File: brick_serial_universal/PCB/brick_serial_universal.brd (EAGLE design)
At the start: 25.4 x 33 mm, 12 parts

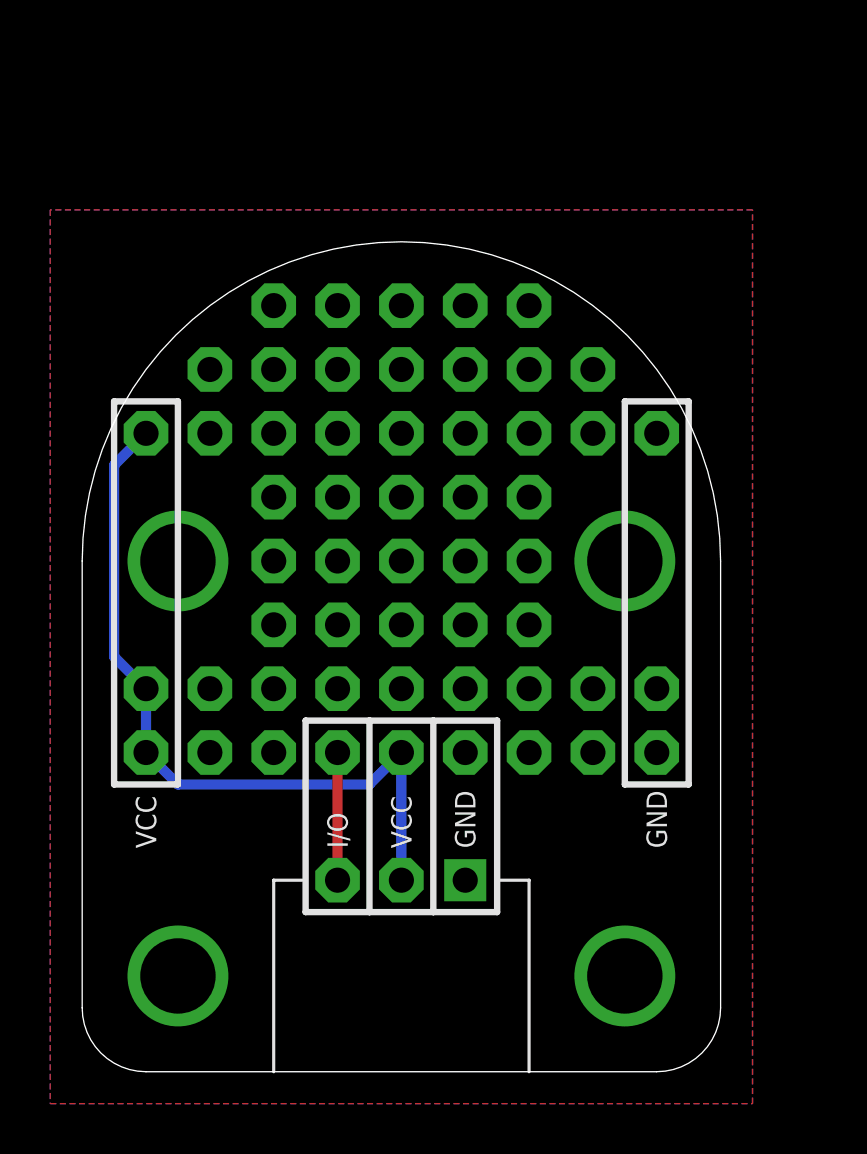
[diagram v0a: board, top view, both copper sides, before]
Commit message: add brick_universal
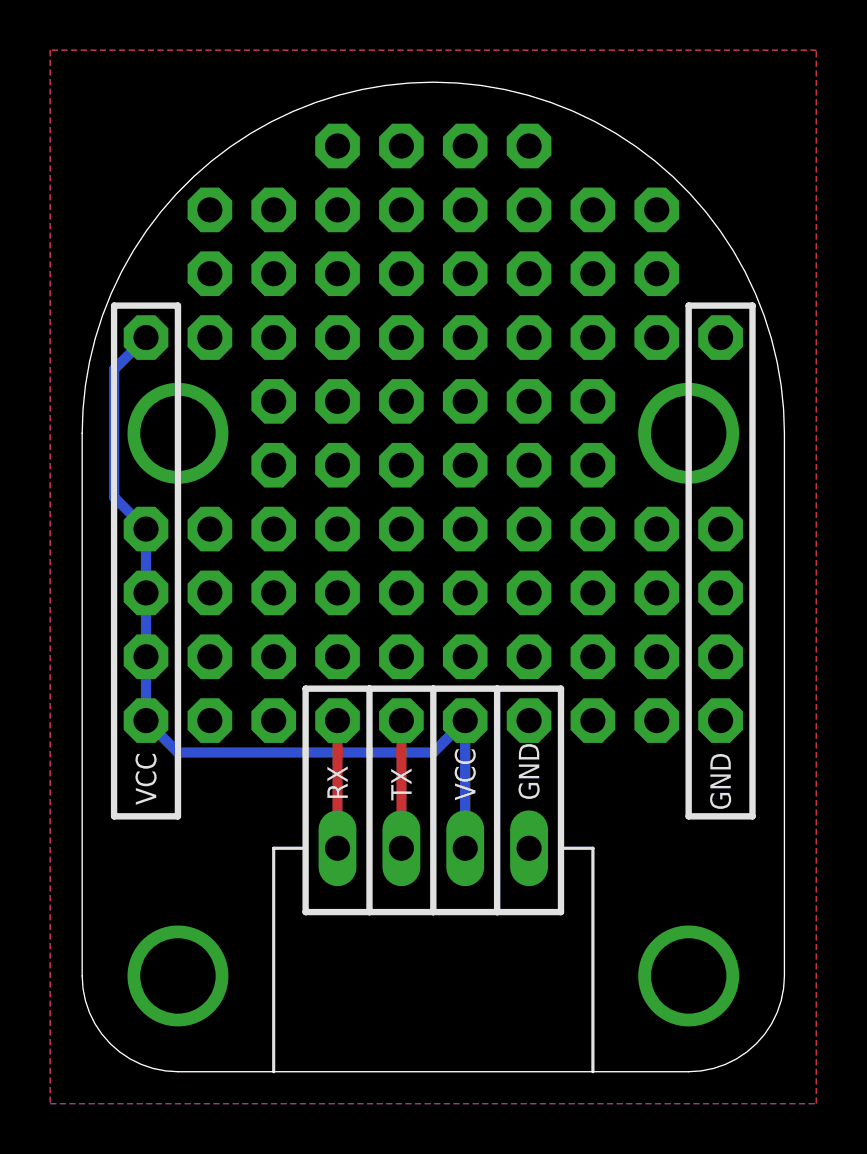
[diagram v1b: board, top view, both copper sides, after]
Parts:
- removed U$1: (no value), FaBo-etc:LOGO_OSHW_S_BOTTOM
- added J11, J12, J13, J14, J15: (no value), FaBo-etc:PIN_1X1_NONAME
- added U$2: (no value), FaBo-etc:LOGO_OSHW_S_BOTTOM
- J1: device FaBo-Template:FABO_BRICK_3PIN_UNIVERSAL -> FaBo-Template:FABO_BRICK_SERIAL_UNIVERSAL
- moved J9 24.7 mm to (2.54, 29.2)
- moved J8 22.2 mm to (2.54, 21.6)
- moved J7 14.2 mm to (2.54, 19.1)
- moved J4 12.8 mm to (15.2, 14.0)
- moved J6 8.89 mm to (2.54, 16.5)
- moved J10 4.58 mm to (25.4, 29.2)
- moved J1 2.84 mm to (14.0, 19.1)
- moved J2 1.27 mm to (10.2, 14.0)
- moved J3 1.27 mm to (12.7, 14.0)
- moved U$3 1.27 mm to (14.0, 2.54)
- moved J5 1.27 mm to (2.54, 14.0)
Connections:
- removed net IO: J1.IN/OUT, J2.1
- new net RX: J1.RX, J2.1
- new net TX: J1.TX, J3.1
- net GND: now also J11.1, J12.1, J13.1, J14.1, J15.1; no longer J7.1, J8.1, J9.1
- net VCC: now also J7.1, J8.1, J9.1; no longer J3.1
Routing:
- net VCC: track 30.0 -> 35.1 mm
- net TX: track 0.00 -> 5.08 mm
- net RX: track 0.00 -> 5.08 mm
- net IO: track 5.08 -> 0.00 mm
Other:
- board size 25.4 x 33 mm -> 27.9 x 39.4 mm
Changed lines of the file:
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@@
 <board>
 <plain>
+<text x="13.97" y="1.27" size="1.016" layer="22" font="vector" ratio="12" rot="MR0" align="bottom-center">MADE IN JAPAN</text>
+<text x="2.54" y="12.7" size="0.8128" layer="21" font="vector" ratio="12" rot="R270" align="center-left">VCC</text>
+<text x="25.4" y="12.7" size="0.8128" layer="21" font="vector" ratio="12" rot="R270" align="center-left">GND</text>
+<wire x1="8.89" y1="6.35" x2="8.89" y2="15.24" width="0.254" layer="21"/>
+<wire x1="8.89" y1="15.24" x2="11.43" y2="15.24" width="0.254" layer="21"/>
+<wire x1="11.43" y1="15.24" x2="13.97" y2="15.24" width="0.254" layer="21"/>
+<wire x1="13.97" y1="15.24" x2="16.51" y2="15.24" width="0.254" layer="21"/>
+<wire x1="16.51" y1="15.24" x2="19.05" y2="15.24" width="0.254" layer="21"/>
+<wire x1="19.05" y1="15.24" x2="19.05" y2="6.35" width="0.254" layer="21"/>
+<wire x1="19.05" y1="6.35" x2="16.51" y2="6.35" width="0.254" layer="21"/>
 <wire x1="16.51" y1="6.35" x2="13.97" y2="6.35" width="0.254" layer="21"/>
 <wire x1="13.97" y1="6.35" x2="11.43" y2="6.35" width="0.254" layer="21"/>
 <wire x1="11.43" y1="6.35" x2="8.89" y2="6.35" width="0.254" layer="21"/>
-<wire x1="8.89" y1="6.35" x2="8.89" y2="13.97" width="0.254" layer="21"/>
-<wire x1="8.89" y1="13.97" x2="11.43" y2="13.97" width="0.254" layer="21"/>
-<wire x1="11.43" y1="13.97" x2="13.97" y2="13.97" width="0.254" layer="21"/>
-<wire x1="13.97" y1="13.97" x2="16.51" y2="13.97" width="0.254" layer="21"/>
-<wire x1="16.51" y1="13.97" x2="16.51" y2="6.35" width="0.254" layer="21"/>
-<wire x1="13.97" y1="13.97" x2="13.97" y2="6.35" width="0.254" layer="21"/>
-<wire x1="11.43" y1="13.97" x2="11.43" y2="6.35" width="0.254" layer="21"/>
-<wire x1="3.81" y1="26.67" x2="3.81" y2="11.43" width="0.254" layer="21"/>
-<wire x1="3.81" y1="11.43" x2="1.27" y2="11.43" width="0.254" layer="21"/>
-<wire x1="1.27" y1="11.43" x2="1.27" y2="26.67" width="0.254" layer="21"/>
-<wire x1="1.27" y1="26.67" x2="3.81" y2="26.67" width="0.254" layer="21"/>
-<wire x1="21.59" y1="26.67" x2="24.13" y2="26.67" width="0.254" layer="21"/>
-<wire x1="24.13" y1="26.67" x2="24.13" y2="11.43" width="0.254" layer="21"/>
-<wire x1="24.13" y1="11.43" x2="21.59" y2="11.43" width="0.254" layer="21"/>
-<wire x1="21.59" y1="11.43" x2="21.59" y2="26.67" width="0.254" layer="21"/>
-<text x="22.86" y="8.89" size="0.8128" layer="21" font="vector" ratio="12" rot="R90" align="center-left">GND</text>
-<text x="2.54" y="8.89" size="0.8128" layer="21" font="vector" ratio="12" rot="R90" align="center-left">VCC</text>
-<text x="12.7" y="1.27" size="1.016" layer="22" font="vector" ratio="12" rot="MR0" align="bottom-center">MADE IN JAPAN</text>
+<wire x1="11.43" y1="15.24" x2="11.43" y2="6.35" width="0.254" layer="21"/>
+<wire x1="13.97" y1="15.24" x2="13.97" y2="6.35" width="0.254" layer="21"/>
+<wire x1="16.51" y1="15.24" x2="16.51" y2="6.35" width="0.254" layer="21"/>
+<wire x1="24.13" y1="30.48" x2="26.67" y2="30.48" width="0.254" layer="21"/>
+<wire x1="26.67" y1="30.48" x2="26.67" y2="10.16" width="0.254" layer="21"/>
+<wire x1="26.67" y1="10.16" x2="24.13" y2="10.16" width="0.254" layer="21"/>
+<wire x1="24.13" y1="10.16" x2="24.13" y2="30.48" width="0.254" layer="21"/>
+<wire x1="1.27" y1="30.48" x2="3.81" y2="30.48" width="0.254" layer="21"/>
+<wire x1="3.81" y1="30.48" x2="3.81" y2="10.16" width="0.254" layer="21"/>
+<wire x1="3.81" y1="10.16" x2="1.27" y2="10.16" width="0.254" layer="21"/>
+<wire x1="1.27" y1="10.16" x2="1.27" y2="30.48" width="0.254" layer="21"/>
 </plain>
 <attributes>
@@
 </autorouter>
 <elements>
-<element name="J1" library="FaBo-Template" package="FABO_BRICK_3PIN_UNIVERSAL" value="" x="12.7" y="16.51"/>
-<element name="J2" library="FaBo-etc" package="PIN_1X1_NONAME" value="" x="10.16" y="12.7"/>
-<element name="J3" library="FaBo-etc" package="PIN_1X1_NONAME" value="" x="12.7" y="12.7"/>
-<element name="J4" library="FaBo-etc" package="PIN_1X1_NONAME" value="" x="2.54" y="12.7"/>
-<element name="J5" library="FaBo-etc" package="PIN_1X1_NONAME" value="" x="2.54" y="15.24"/>
-<element name="J6" library="FaBo-etc" package="PIN_1X1_NONAME" value="" x="2.54" y="25.4"/>
-<element name="J7" library="FaBo-etc" package="PIN_1X1_NONAME" value="" x="15.24" y="12.7"/>
-<element name="J8" library="FaBo-etc" package="PIN_1X1_NONAME" value="" x="22.86" y="12.7"/>
-<element name="J9" library="FaBo-etc" package="PIN_1X1_NONAME" value="" x="22.86" y="15.24"/>
-<element name="J10" library="FaBo-etc" package="PIN_1X1_NONAME" value="" x="22.86" y="25.4"/>
-<element name="U$1" library="FaBo-etc" package="LOGO_OSHW_S_BOTTOM" value="" x="21.59" y="8.89"/>
-<element name="U$3" library="FaBo-etc" package="LOGO_FABO_M_BOTTOM" value="" x="12.7" y="2.54"/>
+<element name="J1" library="FaBo-Template" package="FABO_BRICK_SERIAL_UNIVERSAL" value="" x="13.97" y="19.05"/>
+<element name="J10" library="FaBo-etc" package="PIN_1X1_NONAME" value="" x="25.4" y="29.21"/>
+<element name="J11" library="FaBo-etc" package="PIN_1X1_NONAME" value="" x="25.4" y="21.59"/>
+<element name="J12" library="FaBo-etc" package="PIN_1X1_NONAME" value="" x="25.4" y="19.05"/>
+<element name="J13" library="FaBo-etc" package="PIN_1X1_NONAME" value="" x="17.78" y="13.97"/>
+<element name="J14" library="FaBo-etc" package="PIN_1X1_NONAME" value="" x="25.4" y="13.97"/>
+<element name="J15" library="FaBo-etc" package="PIN_1X1_NONAME" value="" x="25.4" y="16.51"/>
+<element name="J2" library="FaBo-etc" package="PIN_1X1_NONAME" value="" x="10.16" y="13.97"/>
+<element name="J3" library="FaBo-etc" package="PIN_1X1_NONAME" value="" x="12.7" y="13.97"/>
+<element name="J4" library="FaBo-etc" package="PIN_1X1_NONAME" value="" x="15.24" y="13.97"/>
+<element name="J5" library="FaBo-etc" package="PIN_1X1_NONAME" value="" x="2.54" y="13.97"/>
+<element name="J6" library="FaBo-etc" package="PIN_1X1_NONAME" value="" x="2.54" y="16.51"/>
+<element name="J7" library="FaBo-etc" package="PIN_1X1_NONAME" value="" x="2.54" y="19.05"/>
+<element name="J8" library="FaBo-etc" package="PIN_1X1_NONAME" value="" x="2.54" y="21.59"/>
+<element name="J9" library="FaBo-etc" package="PIN_1X1_NONAME" value="" x="2.54" y="29.21"/>
+<element name="U$2" library="FaBo-etc" package="LOGO_OSHW_S_BOTTOM" value="" x="24.13" y="8.89"/>
+<element name="U$3" library="FaBo-etc" package="LOGO_FABO_M_BOTTOM" value="" x="13.97" y="2.54"/>
 </elements>
 <signals>
-<signal name="GND">
-<polygon width="0.4064" layer="1" spacing="0.254">
-<vertex x="-1.27" y="-1.27"/>
-<vertex x="26.67" y="-1.27"/>
-<vertex x="26.67" y="34.29"/>
-<vertex x="-1.27" y="34.29"/>
-</polygon>
-<polygon width="0.4064" layer="16" spacing="0.254">
-<vertex x="-1.27" y="-1.27"/>
-<vertex x="26.67" y="-1.27"/>
-<vertex x="26.67" y="34.29"/>
-<vertex x="-1.27" y="34.29"/>
-</polygon>
-<contactref element="J1" pad="GND"/>
+<signal name="RX">
+<contactref element="J1" pad="RX"/>
+<contactref element="J2" pad="1"/>
+<wire x1="10.16" y1="8.89" x2="10.16" y2="13.97" width="0.4064" layer="1"/>
+</signal>
+<signal name="TX">
+<contactref element="J1" pad="TX"/>
+<contactref element="J3" pad="1"/>
+<wire x1="12.7" y1="13.97" x2="12.7" y2="8.89" width="0.4064" layer="1"/>
+</signal>
+<signal name="VCC">
+<contactref element="J1" pad="VCC"/>
+<contactref element="J4" pad="1"/>
+<contactref element="J5" pad="1"/>
+<contactref element="J6" pad="1"/>
 <contactref element="J7" pad="1"/>
 <contactref element="J8" pad="1"/>
 <contactref element="J9" pad="1"/>
+<wire x1="15.24" y1="8.89" x2="15.24" y2="13.97" width="0.4064" layer="16"/>
+<wire x1="15.24" y1="13.97" x2="13.97" y2="12.7" width="0.4064" layer="16"/>
+<wire x1="13.97" y1="12.7" x2="3.81" y2="12.7" width="0.4064" layer="16"/>
+<wire x1="3.81" y1="12.7" x2="2.54" y2="13.97" width="0.4064" layer="16"/>
+<wire x1="2.54" y1="13.97" x2="2.54" y2="16.51" width="0.4064" layer="16"/>
+<wire x1="2.54" y1="16.51" x2="2.54" y2="19.05" width="0.4064" layer="16"/>
+<wire x1="2.54" y1="19.05" x2="2.54" y2="21.59" width="0.4064" layer="16"/>
+<wire x1="2.54" y1="29.21" x2="1.27" y2="27.94" width="0.4064" layer="16"/>
+<wire x1="1.27" y1="27.94" x2="1.27" y2="22.86" width="0.4064" layer="16"/>
+<wire x1="1.27" y1="22.86" x2="2.54" y2="21.59" width="0.4064" layer="16"/>
+</signal>
+<signal name="GND">
+<contactref element="J1" pad="GND"/>
 <contactref element="J10" pad="1"/>
-</signal>
-<signal name="IO">
-<contactref element="J1" pad="IN/OUT"/>
-<contactref element="J2" pad="1"/>
-<wire x1="10.16" y1="12.7" x2="10.16" y2="7.62" width="0.4064" layer="1"/>
-</signal>
-<signal name="VCC">
-<contactref element="J1" pad="VCC"/>
-<contactref element="J3" pad="1"/>
-<contactref element="J4" pad="1"/>
-<contactref element="J5" pad="1"/>
-<contactref element="J6" pad="1"/>
-<wire x1="12.7" y1="7.62" x2="12.7" y2="12.7" width="0.4064" layer="16"/>
-<wire x1="12.7" y1="12.7" x2="11.43" y2="11.43" width="0.4064" layer="16"/>
-<wire x1="11.43" y1="11.43" x2="3.81" y2="11.43" width="0.4064" layer="16"/>
-<wire x1="3.81" y1="11.43" x2="2.54" y2="12.7" width="0.4064" layer="16"/>
-<wire x1="2.54" y1="12.7" x2="2.54" y2="15.24" width="0.4064" layer="16"/>
-<wire x1="2.54" y1="25.4" x2="1.27" y2="24.13" width="0.4064" layer="16"/>
-<wire x1="1.27" y1="24.13" x2="1.27" y2="16.51" width="0.4064" layer="16"/>
-<wire x1="1.27" y1="16.51" x2="2.54" y2="15.24" width="0.4064" layer="16"/>
+<contactref element="J11" pad="1"/>
+<contactref element="J12" pad="1"/>
+<contactref element="J13" pad="1"/>
+<contactref element="J14" pad="1"/>
+<contactref element="J15" pad="1"/>
+<polygon width="0.4064" layer="16" spacing="0.254">
+<vertex x="-1.27" y="-1.27"/>
+<vertex x="29.21" y="-1.27"/>
+<vertex x="29.21" y="40.64"/>
+<vertex x="-1.27" y="40.64"/>
+</polygon>
+<polygon width="0.4064" layer="1" spacing="0.254">
+<vertex x="-1.27" y="-1.27"/>
+<vertex x="29.21" y="-1.27"/>
+<vertex x="29.21" y="40.64"/>
+<vertex x="-1.27" y="40.64"/>
+</polygon>
 </signal>
 </signals>

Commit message: change Revision
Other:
- board text added: "Rev.1.0.0"
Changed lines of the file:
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@@
 <wire x1="3.81" y1="10.16" x2="1.27" y2="10.16" width="0.254" layer="21"/>
 <wire x1="1.27" y1="10.16" x2="1.27" y2="30.48" width="0.254" layer="21"/>
+<text x="1.27" y="6.35" size="0.8128" layer="22" font="vector" ratio="12" rot="MR90">Rev.1.0.0</text>
 </plain>
 <attributes>
